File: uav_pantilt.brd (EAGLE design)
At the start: 58.1 x 27.9 mm, 12 parts

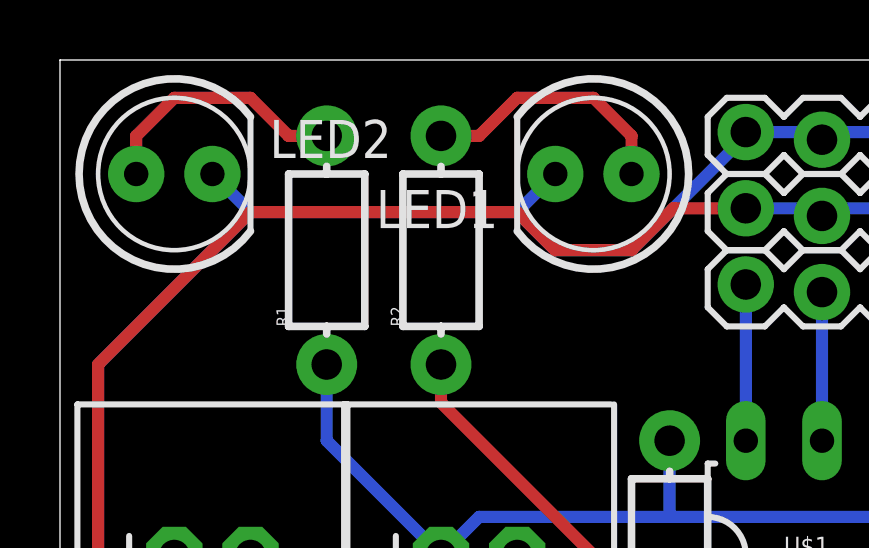
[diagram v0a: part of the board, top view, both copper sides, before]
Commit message: Added reset resistor, added power and BUSY led.
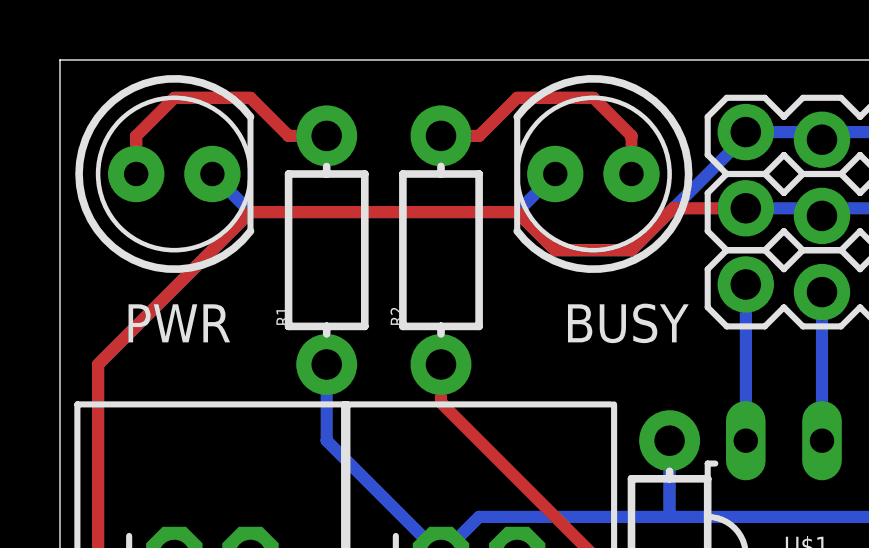
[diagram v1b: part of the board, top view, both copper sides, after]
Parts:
- renumbered LED1 to BUSY, LED2 to PWR
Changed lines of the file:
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@@
 <element name="R1" library="SparkFun-Resistors" package="AXIAL-0.3-KIT" value="" x="8.89" y="21.59" rot="R90"/>
 <element name="R2" library="SparkFun-Resistors" package="AXIAL-0.3-KIT" value="" x="12.7" y="21.59" rot="R90"/>
-<element name="LED1" library="SparkFun-LED" package="LED5MM" value="" x="17.78" y="24.13" rot="R180"/>
-<element name="LED2" library="SparkFun-LED" package="LED5MM" value="" x="3.81" y="24.13"/>
+<element name="BUSY" library="SparkFun-LED" package="LED5MM" value="" x="17.78" y="24.13" smashed="yes" rot="R180">
+<attribute name="NAME" x="20.955" y="19.7866" size="1.27" layer="25" ratio="10" rot="R180"/>
+<attribute name="VALUE" x="14.5796" y="25.9334" size="1.27" layer="27" ratio="10" rot="R180"/>
+</element>
+<element name="PWR" library="SparkFun-LED" package="LED5MM" value="" x="3.81" y="24.13" smashed="yes">
+<attribute name="NAME" x="5.715" y="19.7866" size="1.27" layer="25" ratio="10" rot="R180"/>
+<attribute name="VALUE" x="7.0104" y="22.3266" size="1.27" layer="27" ratio="10"/>
+</element>
 <element name="R3" library="SparkFun-Resistors" package="AXIAL-0.3-KIT" value="" x="20.32" y="11.43" rot="R90"/>
 </elements>
@@
 <wire x1="40.64" y1="10.16" x2="41.91" y2="11.43" width="0.4064" layer="1"/>
 <wire x1="41.91" y1="11.43" x2="44.45" y2="11.43" width="0.4064" layer="1"/>
-<contactref element="LED2" pad="K"/>
-<contactref element="LED1" pad="K"/>
+<contactref element="PWR" pad="K"/>
+<contactref element="BUSY" pad="K"/>
 <wire x1="3.81" y1="6.35" x2="1.27" y2="8.89" width="0.4064" layer="16"/>
 <wire x1="1.27" y1="8.89" x2="1.27" y2="17.78" width="0.4064" layer="16"/>
@@
 </signal>
 <signal name="N$1">
-<contactref element="LED2" pad="A"/>
+<contactref element="PWR" pad="A"/>
 <contactref element="R1" pad="P$2"/>
 <wire x1="8.89" y1="25.4" x2="7.62" y2="25.4" width="0.4064" layer="1"/>
@@
 </signal>
 <signal name="N$2">
-<contactref element="LED1" pad="A"/>
+<contactref element="BUSY" pad="A"/>
 <contactref element="R2" pad="P$2"/>
 <wire x1="12.7" y1="25.4" x2="13.97" y2="25.4" width="0.4064" layer="1"/>

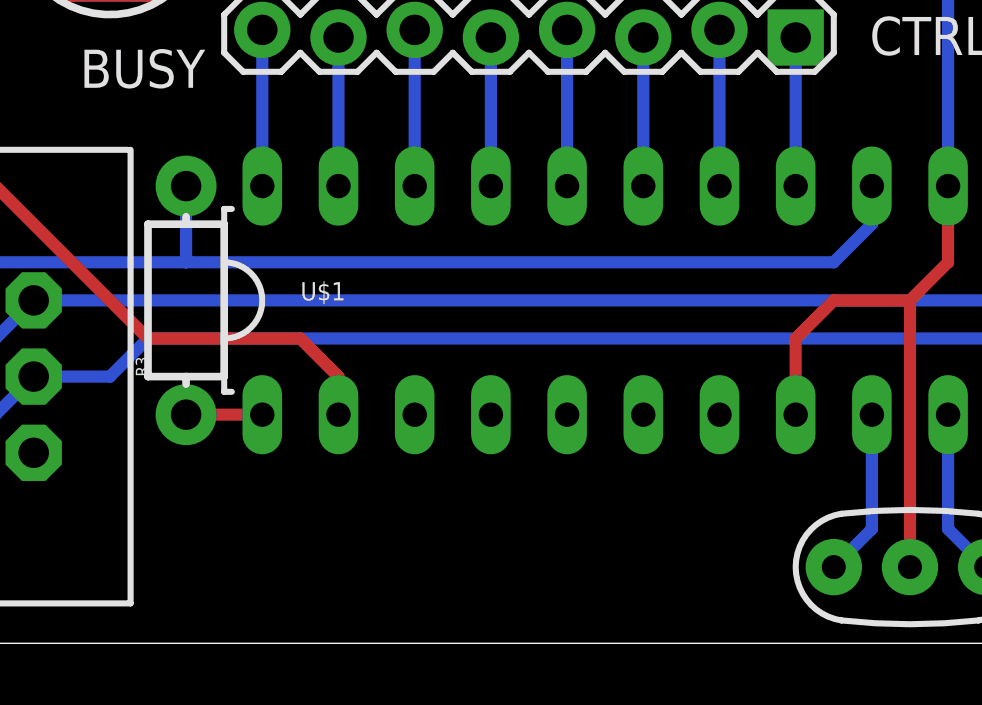
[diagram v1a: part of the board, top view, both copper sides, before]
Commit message: Adding ICSP to Pantilt board
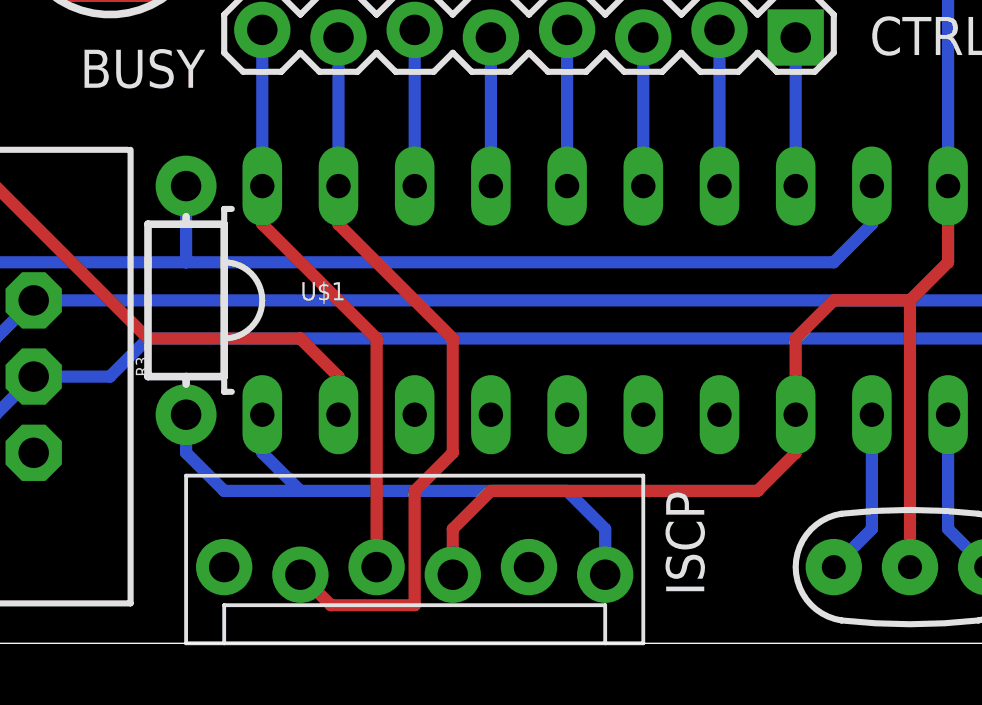
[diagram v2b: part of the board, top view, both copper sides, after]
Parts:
- added ISCP: (no value), SparkFun-Connectors:MOLEX-1X6_LOCK
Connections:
- removed net RST: R3.P$1, U$1.1
- new net MCLR: ISCP.6, R3.P$1, U$1.1
- new net VCC_NC: ISCP.5
- net GND: now also ISCP.4
- net SRV_7: now also ISCP.2
- net SRV_8: now also ISCP.3
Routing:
- net MCLR: track 0.00 -> 20.9 mm
- net SRV_7: track 4.95 -> 25.3 mm
- net GND: track 105.3 -> 120.6 mm
- net SRV_8: track 5.21 -> 19.5 mm
- net RST: track 2.54 -> 0.00 mm
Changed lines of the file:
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@@
 </element>
 <element name="R3" library="SparkFun-Resistors" package="AXIAL-0.3-KIT" value="" x="20.32" y="11.43" rot="R90"/>
+<element name="ISCP" library="SparkFun-Connectors" package="MOLEX-1X6_LOCK" value="" x="21.59" y="2.54" smashed="yes">
+<attribute name="NAME" x="36.322" y="5.08" size="1.27" layer="25" font="vector" rot="R270"/>
+<attribute name="VALUE" x="20.32" y="-1.524" size="1.27" layer="27" font="vector"/>
+</element>
 </elements>
 <signals>
@@
 <wire x1="19.05" y1="21.59" x2="16.51" y2="21.59" width="0.4064" layer="16"/>
 <wire x1="16.51" y1="21.59" x2="15.24" y2="22.86" width="0.4064" layer="16"/>
+<contactref element="ISCP" pad="4"/>
+<wire x1="29.21" y1="2.286" x2="29.21" y2="3.81" width="0.4064" layer="1"/>
+<wire x1="29.21" y1="3.81" x2="30.48" y2="5.08" width="0.4064" layer="1"/>
+<wire x1="30.48" y1="5.08" x2="39.37" y2="5.08" width="0.4064" layer="1"/>
+<wire x1="39.37" y1="5.08" x2="40.64" y2="6.35" width="0.4064" layer="1"/>
+<wire x1="40.64" y1="6.35" x2="40.64" y2="7.62" width="0.4064" layer="1"/>
 </signal>
 <signal name="5V">
@@
 <contactref element="CTRL" pad="7"/>
 <wire x1="25.4" y1="15.24" x2="25.4" y2="20.193" width="0.4064" layer="16"/>
+<contactref element="ISCP" pad="2"/>
+<wire x1="25.4" y1="15.24" x2="25.4" y2="13.97" width="0.4064" layer="1"/>
+<wire x1="25.4" y1="13.97" x2="29.21" y2="10.16" width="0.4064" layer="1"/>
+<wire x1="29.21" y1="10.16" x2="29.21" y2="6.35" width="0.4064" layer="1"/>
+<wire x1="29.21" y1="6.35" x2="27.94" y2="5.08" width="0.4064" layer="1"/>
+<wire x1="27.94" y1="5.08" x2="27.94" y2="1.27" width="0.4064" layer="1"/>
+<wire x1="27.94" y1="1.27" x2="25.146" y2="1.27" width="0.4064" layer="1"/>
+<wire x1="25.146" y1="1.27" x2="24.13" y2="2.286" width="0.4064" layer="1"/>
 </signal>
 <signal name="SRV_8">
@@
 <contactref element="CTRL" pad="8"/>
 <wire x1="22.86" y1="15.24" x2="22.86" y2="20.447" width="0.4064" layer="16"/>
+<contactref element="ISCP" pad="3"/>
+<wire x1="22.86" y1="15.24" x2="22.86" y2="13.97" width="0.4064" layer="1"/>
+<wire x1="22.86" y1="13.97" x2="26.67" y2="10.16" width="0.4064" layer="1"/>
+<wire x1="26.67" y1="10.16" x2="26.67" y2="2.54" width="0.4064" layer="1"/>
 </signal>
 <signal name="N$1">
@@
 <wire x1="19.05" y1="25.4" x2="19.05" y2="24.13" width="0.4064" layer="1"/>
 </signal>
-<signal name="RST">
-<contactref element="U$1" pad="1"/>
-<contactref element="R3" pad="P$1"/>
-<wire x1="20.32" y1="7.62" x2="22.86" y2="7.62" width="0.4064" layer="1"/>
-</signal>
 <signal name="BSY">
 <contactref element="U$1" pad="2"/>
@@
 <wire x1="25.4" y1="8.89" x2="25.4" y2="7.62" width="0.4064" layer="1"/>
 </signal>
+<signal name="MCLR">
+<contactref element="ISCP" pad="6"/>
+<contactref element="U$1" pad="1"/>
+<contactref element="R3" pad="P$1"/>
+<wire x1="34.29" y1="2.286" x2="34.29" y2="3.81" width="0.4064" layer="16"/>
+<wire x1="34.29" y1="3.81" x2="33.02" y2="5.08" width="0.4064" layer="16"/>
+<wire x1="33.02" y1="5.08" x2="24.13" y2="5.08" width="0.4064" layer="16"/>
+<wire x1="24.13" y1="5.08" x2="22.86" y2="6.35" width="0.4064" layer="16"/>
+<wire x1="22.86" y1="6.35" x2="22.86" y2="7.62" width="0.4064" layer="16"/>
+<wire x1="20.32" y1="7.62" x2="20.32" y2="6.35" width="0.4064" layer="16"/>
+<wire x1="20.32" y1="6.35" x2="21.59" y2="5.08" width="0.4064" layer="16"/>
+<wire x1="21.59" y1="5.08" x2="24.13" y2="5.08" width="0.4064" layer="16"/>
+</signal>
+<signal name="VCC_NC">
+<contactref element="ISCP" pad="5"/>
+</signal>
 </signals>
